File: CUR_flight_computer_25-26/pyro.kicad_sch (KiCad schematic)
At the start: 26 parts, among them J10 PYRO, J11 PYRO, J8 PYRO, J9 PYRO, U12 BUK9K25-40RAX, U13 BUK9K25-40RAX

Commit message: more more organization
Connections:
- net at R31.2, R33.1: now also U13.2 (G1); no longer U12.4 (G2)
- net at J9.1 (Pin_1), R36.1: now also U13.5 (D1); no longer U12.6 (D2)
- net at R38.2, R40.1: now also U12.4 (G2); no longer U13.2 (G1)
- net at J10.1 (Pin_1), R42.1: now also U12.6 (D2); no longer U13.5 (D1)
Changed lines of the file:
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@@
-	)
-	(symbol
-		(lib_id "BUK9K25-40RAX:BUK9K25-40RAX")
-		(at 74.93 140.97 0)
-		(unit 2)
-		(exclude_from_sim no)
-		(in_bom yes)
-		(on_board yes)
-		(dnp no)
-		(property "Reference" "U12"
-			(at 78.994 147.32 90)
-			(effects
-				(font
-					(size 1.27 1.27)
-				)
-				(justify left)
-			)
-		)
-		(property "Value" "BUK9K25-40RAX"
-			(at 81.534 147.32 90)
-			(effects
-				(font
-					(size 1.27 1.27)
-				)
-				(justify left)
-			)
-		)
-		(property "Footprint" "BUK9K25-40RAX:BUK9K2540RAX"
-			(at 74.93 140.97 0)
-			(effects
-				(font
-					(size 1.27 1.27)
-				)
-				(hide yes)
-			)
-		)
-		(property "Datasheet" "https://assets.nexperia.com/documents/data-sheet/BUK9K25-40RA.pdf"
-			(at 74.93 140.97 0)
-			(effects
-				(font
-					(size 1.27 1.27)
-				)
-				(hide yes)
-			)
-		)
-		(property "Description" "Nexperia USA Mosfet Array 40V 18.2A 2 N Channel NMOS"
-			(at 74.93 140.97 0)
-			(effects
-				(font
-					(size 1.27 1.27)
-				)
-				(hide yes)
-			)
-		)
-		(pin "4"
-		)
-		(pin "6"
-		)
-		(pin "1"
-		)
-		(pin "5"
-		)
-		(pin "3"
-		)
-		(pin "2"
-		)
-		(instances
-			(project ""
-				(path "/bf7761cc-1b32-4d86-809c-5f027005229b/a6095a4d-1542-4c9d-ab0b-9ed076818c96"
-					(reference "U12")
-					(unit 2)
-				)
-			)
-		)
 	)
 	(symbol
@@
 	(symbol
 		(lib_id "BUK9K25-40RAX:BUK9K25-40RAX")
+		(at 74.93 140.97 0)
+		(unit 1)
+		(exclude_from_sim no)
+		(in_bom yes)
+		(on_board yes)
+		(dnp no)
+		(property "Reference" "U13"
+			(at 79.756 148.082 90)
+			(effects
+				(font
+					(size 1.27 1.27)
+				)
+				(justify left)
+			)
+		)
+		(property "Value" "BUK9K25-40RAX"
+			(at 82.296 148.082 90)
+			(effects
+				(font
+					(size 1.27 1.27)
+				)
+				(justify left)
+			)
+		)
+		(property "Footprint" "BUK9K25-40RAX:BUK9K2540RAX"
+			(at 74.93 140.97 0)
+			(effects
+				(font
+					(size 1.27 1.27)
+				)
+				(hide yes)
+			)
+		)
+		(property "Datasheet" "https://assets.nexperia.com/documents/data-sheet/BUK9K25-40RA.pdf"
+			(at 74.93 140.97 0)
+			(effects
+				(font
+					(size 1.27 1.27)
+				)
+				(hide yes)
+			)
+		)
+		(property "Description" "Nexperia USA Mosfet Array 40V 18.2A 2 N Channel NMOS"
+			(at 74.93 140.97 0)
+			(effects
+				(font
+					(size 1.27 1.27)
+				)
+				(hide yes)
+			)
+		)
+		(pin "4"
+		)
+		(pin "6"
+		)
+		(pin "1"
+		)
+		(pin "5"
+		)
+		(pin "3"
+		)
+		(pin "2"
+		)
+		(instances
+			(project "CUR_flight_computer_25-26"
+				(path "/bf7761cc-1b32-4d86-809c-5f027005229b/a6095a4d-1542-4c9d-ab0b-9ed076818c96"
+					(reference "U13")
+					(unit 1)
+				)
+			)
+		)
+	)
+	(symbol
+		(lib_id "BUK9K25-40RAX:BUK9K25-40RAX")
 		(at 151.13 71.12 0)
-		(unit 1)
-		(exclude_from_sim no)
-		(in_bom yes)
-		(on_board yes)
-		(dnp no)
-		(property "Reference" "U13"
-			(at 155.956 78.232 90)
+		(unit 2)
+		(exclude_from_sim no)
+		(in_bom yes)
+		(on_board yes)
+		(dnp no)
+		(property "Reference" "U12"
+			(at 155.194 77.47 90)
 			(effects
 				(font
@@
 		)
 		(property "Value" "BUK9K25-40RAX"
-			(at 158.496 78.232 90)
+			(at 157.734 77.47 90)
 			(effects
 				(font
@@
 			(project "CUR_flight_computer_25-26"
 				(path "/bf7761cc-1b32-4d86-809c-5f027005229b/a6095a4d-1542-4c9d-ab0b-9ed076818c96"
-					(reference "U13")
-					(unit 1)
-				)
-			)
+					(reference "U12")
+					(unit 2)
+				)
+			)

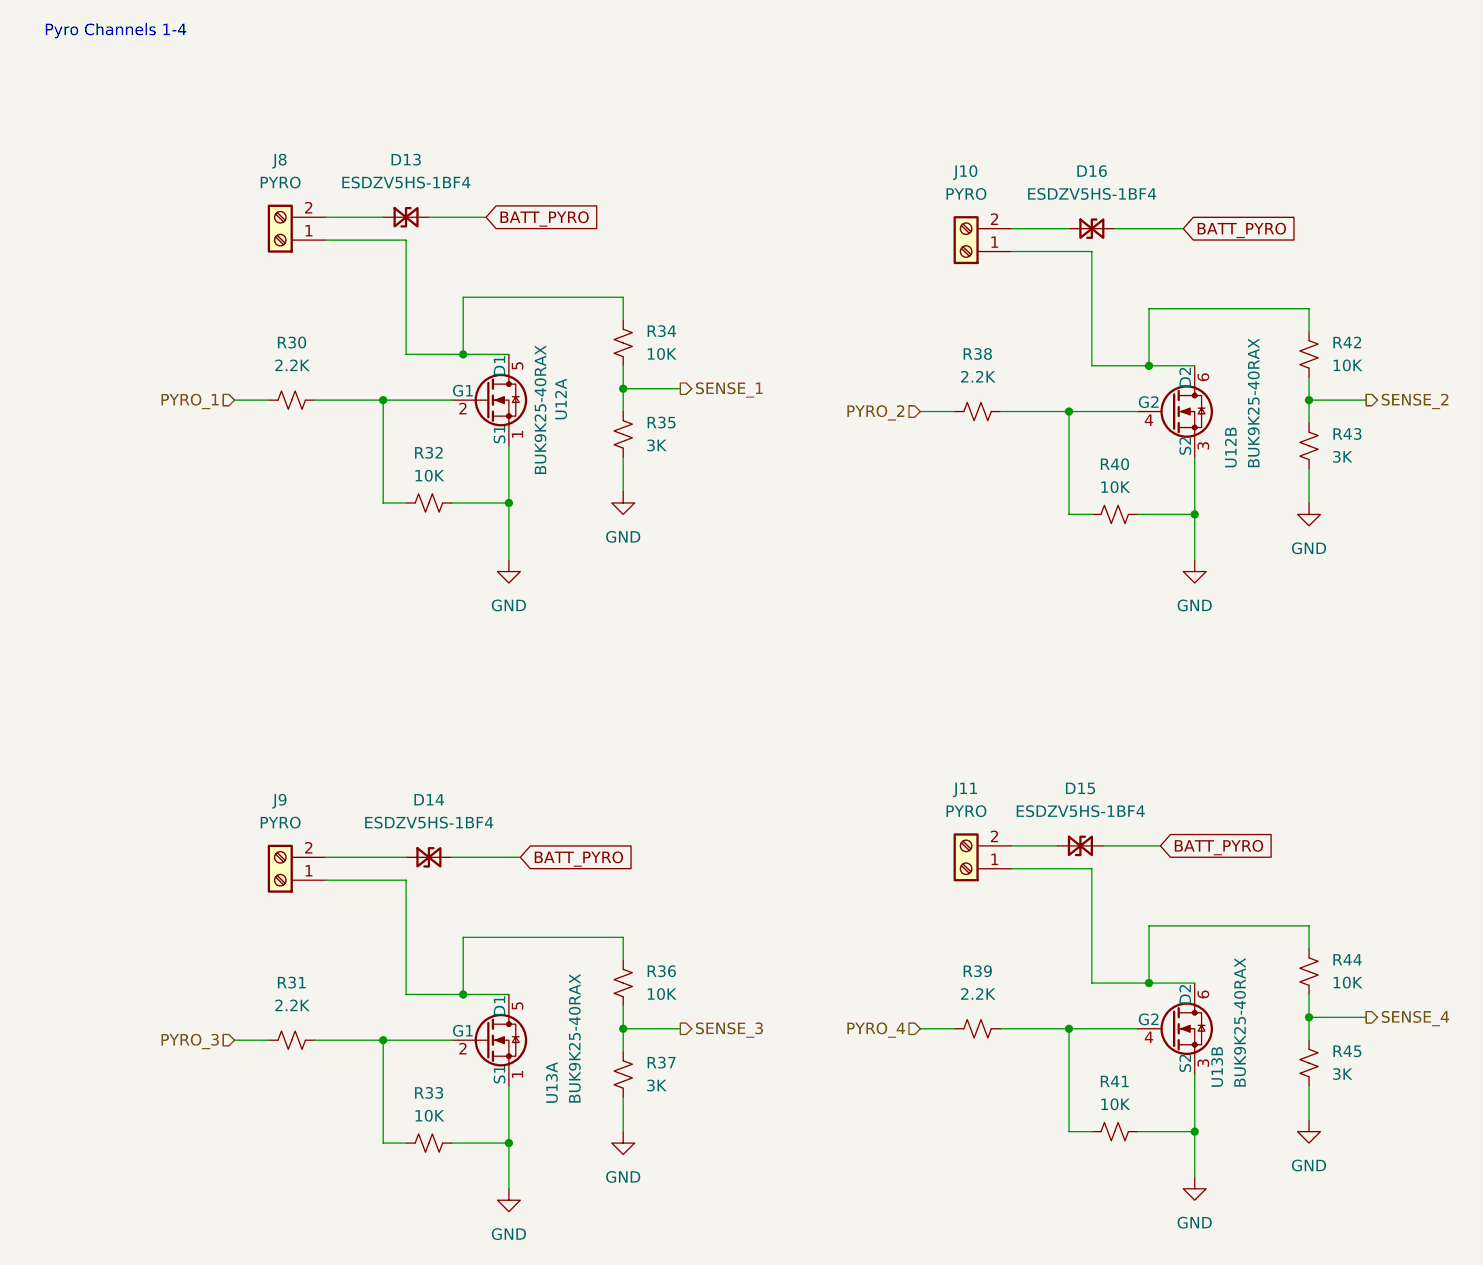
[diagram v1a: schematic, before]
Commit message: most of layout figured out
trouble finding room for power
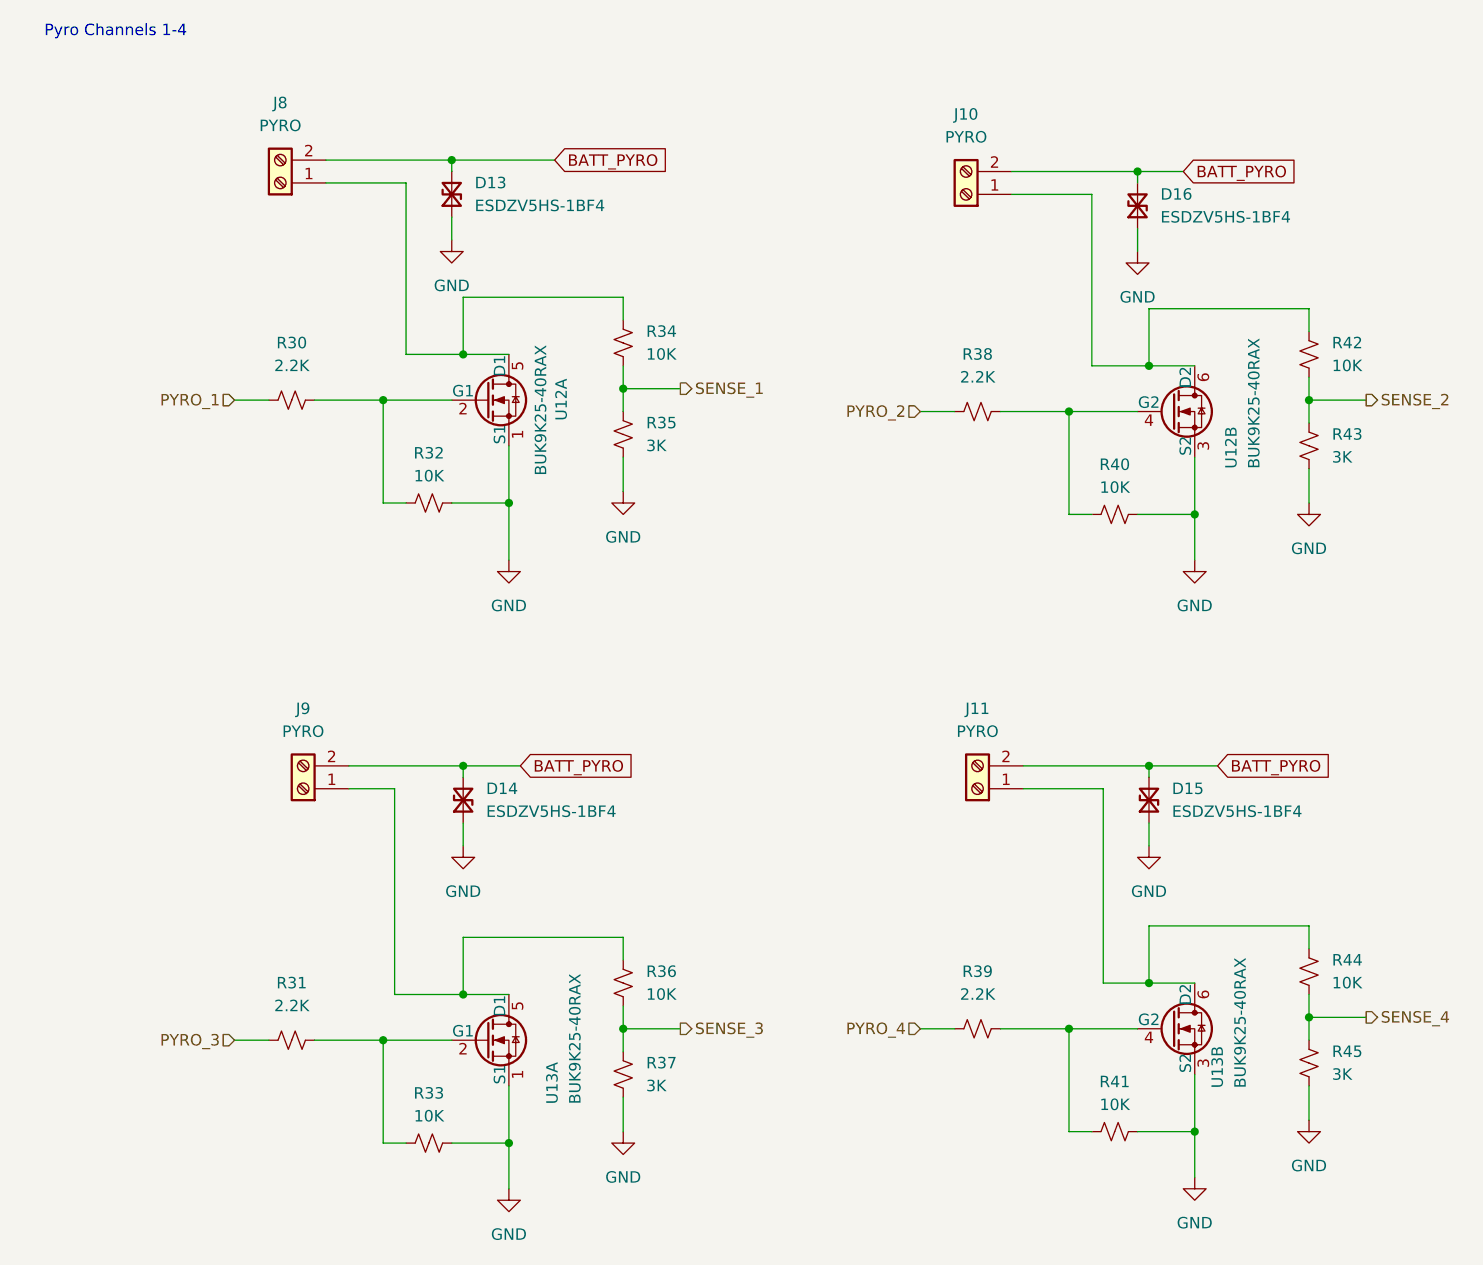
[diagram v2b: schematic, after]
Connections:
- net BATT_PYRO: now also J10.2 (Pin_2), J11.2 (Pin_2), J8.2 (Pin_2), J9.2 (Pin_2)
- net GND: now also D13.1 (A1), D14.1 (A1), D15.1 (A1), D16.1 (A1)
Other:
- moved on the sheet: D13, J10, J11, J8, J9

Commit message: added new header footprint
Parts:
- J10, J11, J8, J9: footprint TerminalBlock_Phoenix:TerminalBlock_Phoenix_PT-1,5-2-5.0-H_1x02_P5.00mm_Horizontal -> Terminal_SAMESKY_TB0011-350-02GR:SAMESKY_TB0011-350-02GR
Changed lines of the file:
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@@
 			)
 		)
-		(property "Footprint" "TerminalBlock_Phoenix:TerminalBlock_Phoenix_PT-1,5-2-5.0-H_1x02_P5.00mm_Horizontal"
+		(property "Footprint" "Terminal_SAMESKY_TB0011-350-02GR:SAMESKY_TB0011-350-02GR"
 			(at 52.07 113.03 0)
 			(effects
@@
 			)
 		)
-		(property "Footprint" "TerminalBlock_Phoenix:TerminalBlock_Phoenix_PT-1,5-2-5.0-H_1x02_P5.00mm_Horizontal"
+		(property "Footprint" "Terminal_SAMESKY_TB0011-350-02GR:SAMESKY_TB0011-350-02GR"
 			(at 49.53 45.72 0)
 			(effects
@@
 			)
 		)
-		(property "Footprint" "TerminalBlock_Phoenix:TerminalBlock_Phoenix_PT-1,5-2-5.0-H_1x02_P5.00mm_Horizontal"
+		(property "Footprint" "Terminal_SAMESKY_TB0011-350-02GR:SAMESKY_TB0011-350-02GR"
 			(at 127 113.03 0)
 			(effects
@@
 			)
 		)
-		(property "Footprint" "TerminalBlock_Phoenix:TerminalBlock_Phoenix_PT-1,5-2-5.0-H_1x02_P5.00mm_Horizontal"
+		(property "Footprint" "Terminal_SAMESKY_TB0011-350-02GR:SAMESKY_TB0011-350-02GR"
 			(at 125.73 46.99 0)
 			(effects

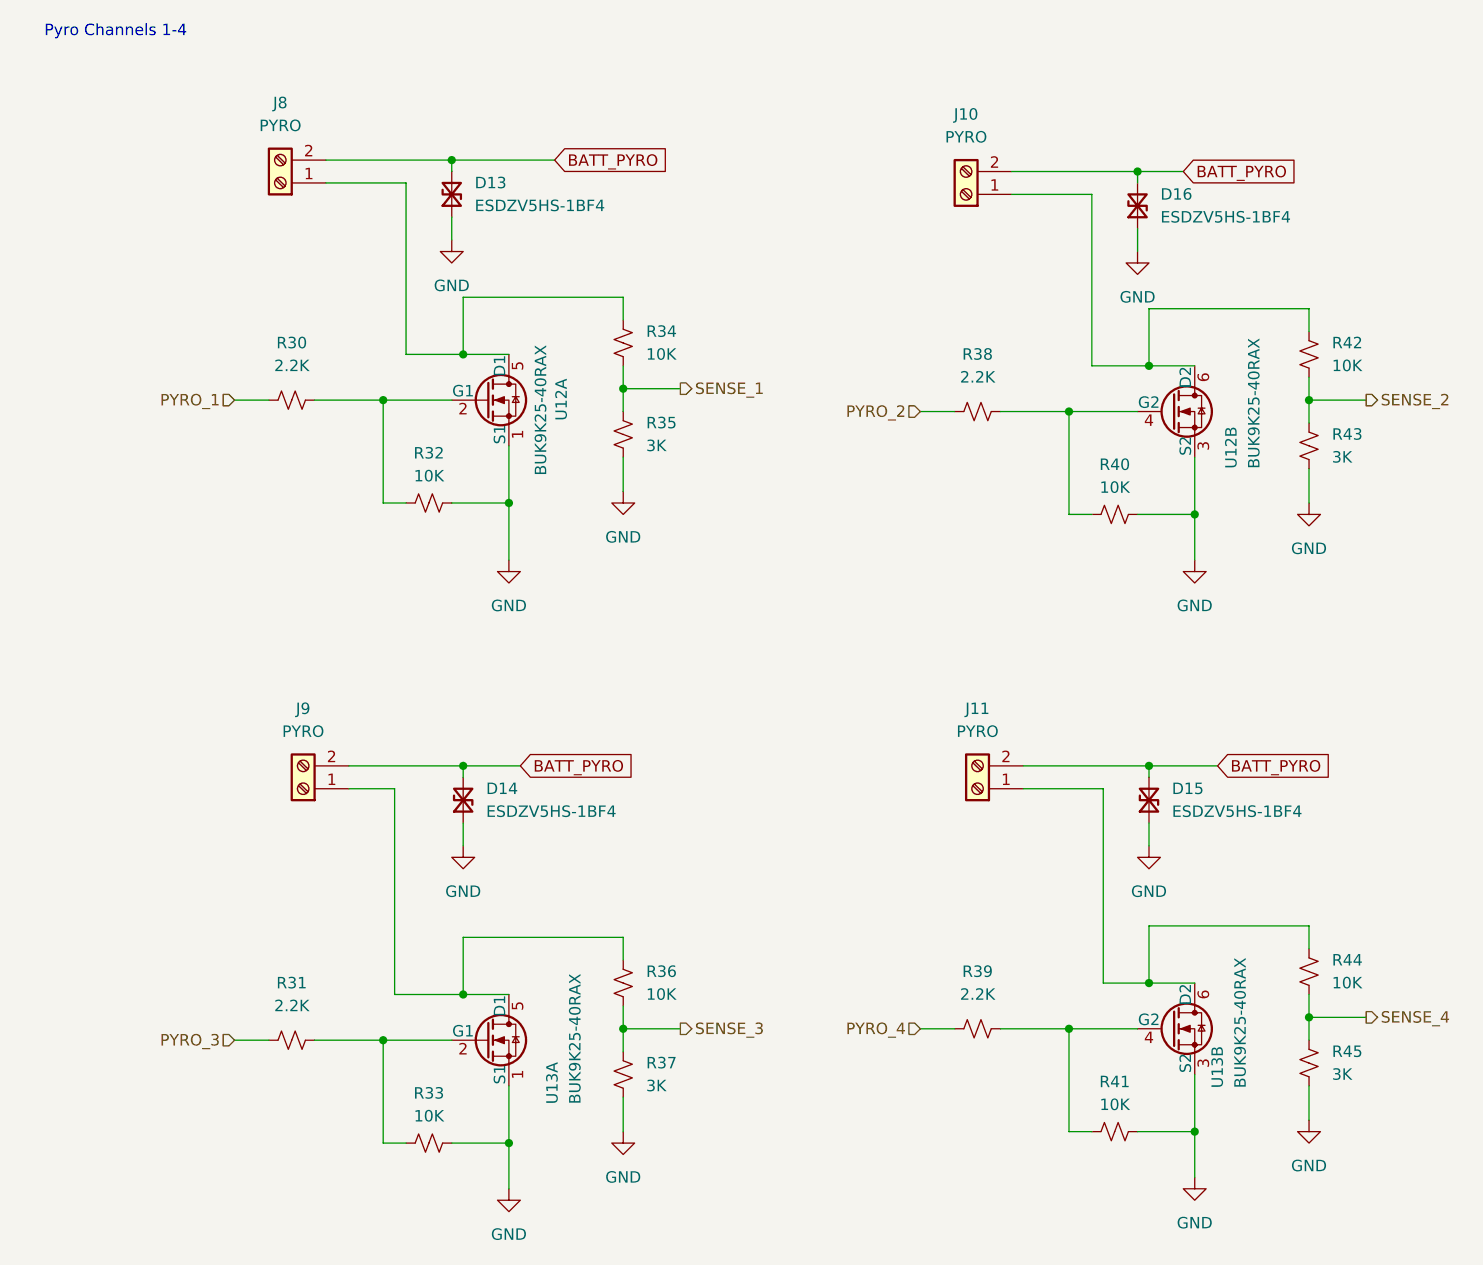
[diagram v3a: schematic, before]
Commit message: updates to tvs diodes
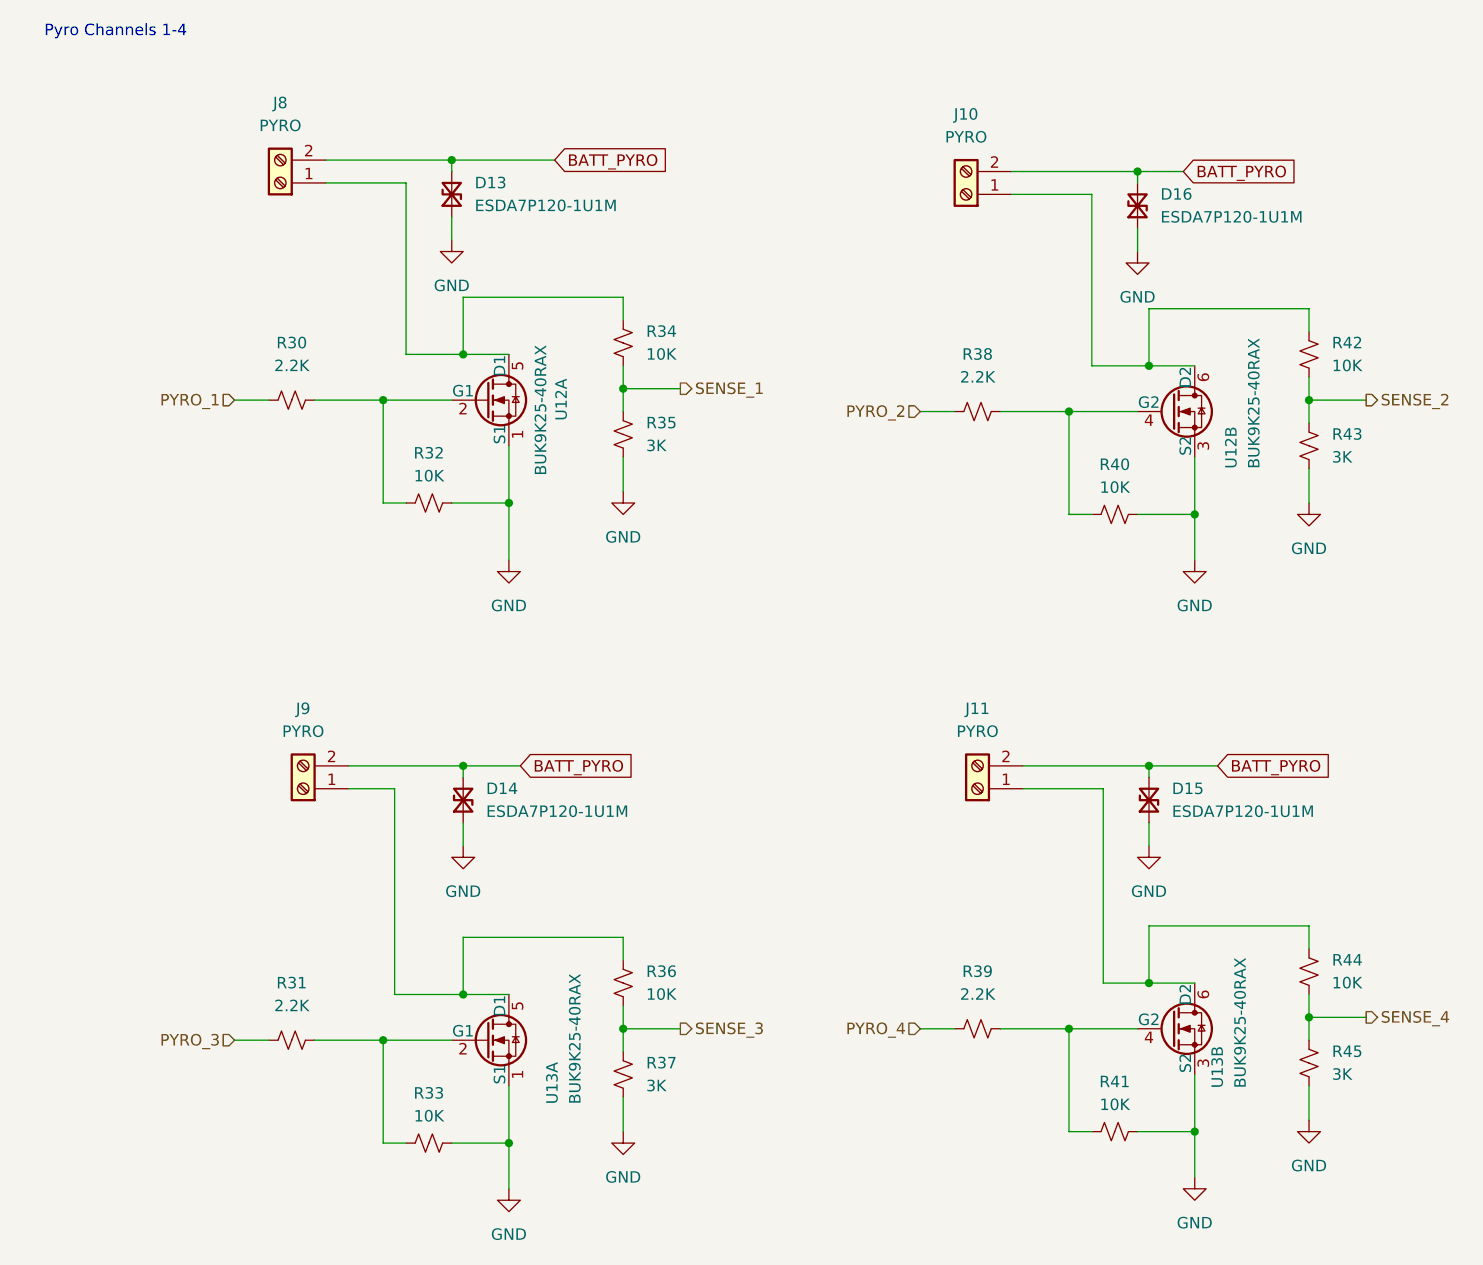
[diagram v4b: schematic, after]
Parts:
- D13, D14, D15, D16: value ESDZV5HS-1BF4 -> ESDA7P120-1U1M
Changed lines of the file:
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@@
 			)
 		)
-		(property "Value" "ESDZV5HS-1BF4"
+		(property "Value" "ESDA7P120-1U1M"
 			(at 148.59 115.5699 90)
 			(effects
@@
 			)
 		)
-		(property "Value" "ESDZV5HS-1BF4"
+		(property "Value" "ESDA7P120-1U1M"
 			(at 147.32 49.5299 90)
 			(effects
@@
 			)
 		)
-		(property "Value" "ESDZV5HS-1BF4"
+		(property "Value" "ESDA7P120-1U1M"
 			(at 72.39 115.5699 90)
 			(effects
@@
 			)
 		)
-		(property "Value" "ESDZV5HS-1BF4"
+		(property "Value" "ESDA7P120-1U1M"
 			(at 71.12 48.2599 90)
 			(effects

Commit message: started traces...yay
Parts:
- D13, D14, D15, D16: footprint Diode_SMD:D_0201_0603Metric -> ESDA7P120:TVS_ESDA7P120-1U1M
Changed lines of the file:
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@@
 			)
 		)
-		(property "Footprint" "Diode_SMD:D_0201_0603Metric"
+		(property "Footprint" "ESDA7P120:TVS_ESDA7P120-1U1M"
 			(at 146.05 114.3 0)
 			(effects
@@
 			)
 		)
-		(property "Footprint" "Diode_SMD:D_0201_0603Metric"
+		(property "Footprint" "ESDA7P120:TVS_ESDA7P120-1U1M"
 			(at 144.78 48.26 0)
 			(effects
@@
 			)
 		)
-		(property "Footprint" "Diode_SMD:D_0201_0603Metric"
+		(property "Footprint" "ESDA7P120:TVS_ESDA7P120-1U1M"
 			(at 69.85 114.3 0)
 			(effects
@@
 			)
 		)
-		(property "Footprint" "Diode_SMD:D_0201_0603Metric"
+		(property "Footprint" "ESDA7P120:TVS_ESDA7P120-1U1M"
 			(at 68.58 46.99 0)
 			(effects
